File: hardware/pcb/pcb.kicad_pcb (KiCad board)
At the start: 2 copper layers, 122 x 122 mm, 50 parts, among them J1 USB_B_Micro, J2 USB_A, J3 USB_A, J4 USB_A, M1 Fan, Q1 S8050, SW1 SW_Push, U1 locked, U2 AT89C52, U3 SL2.1A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

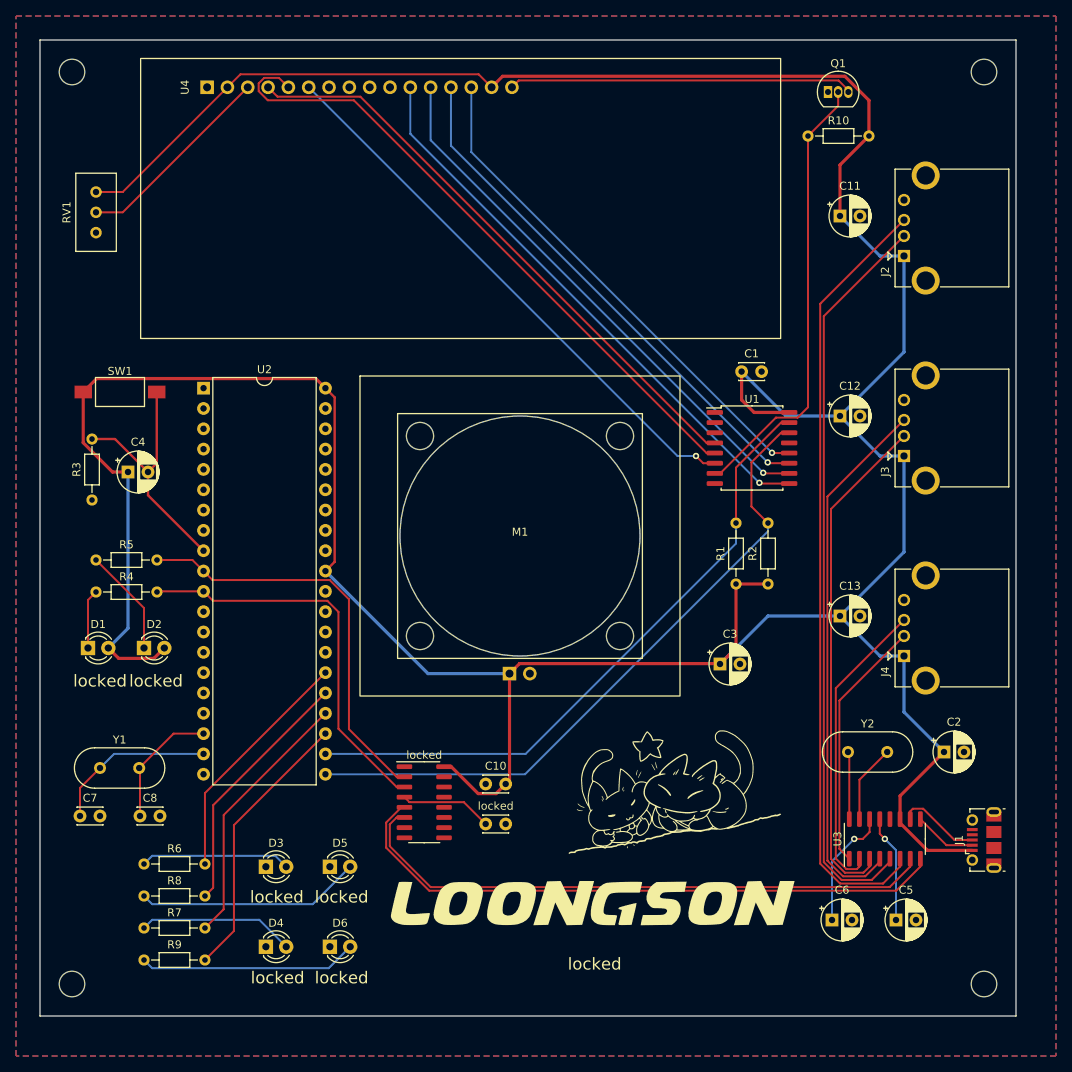
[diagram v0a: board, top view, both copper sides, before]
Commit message: Update KiCAD to 8.0
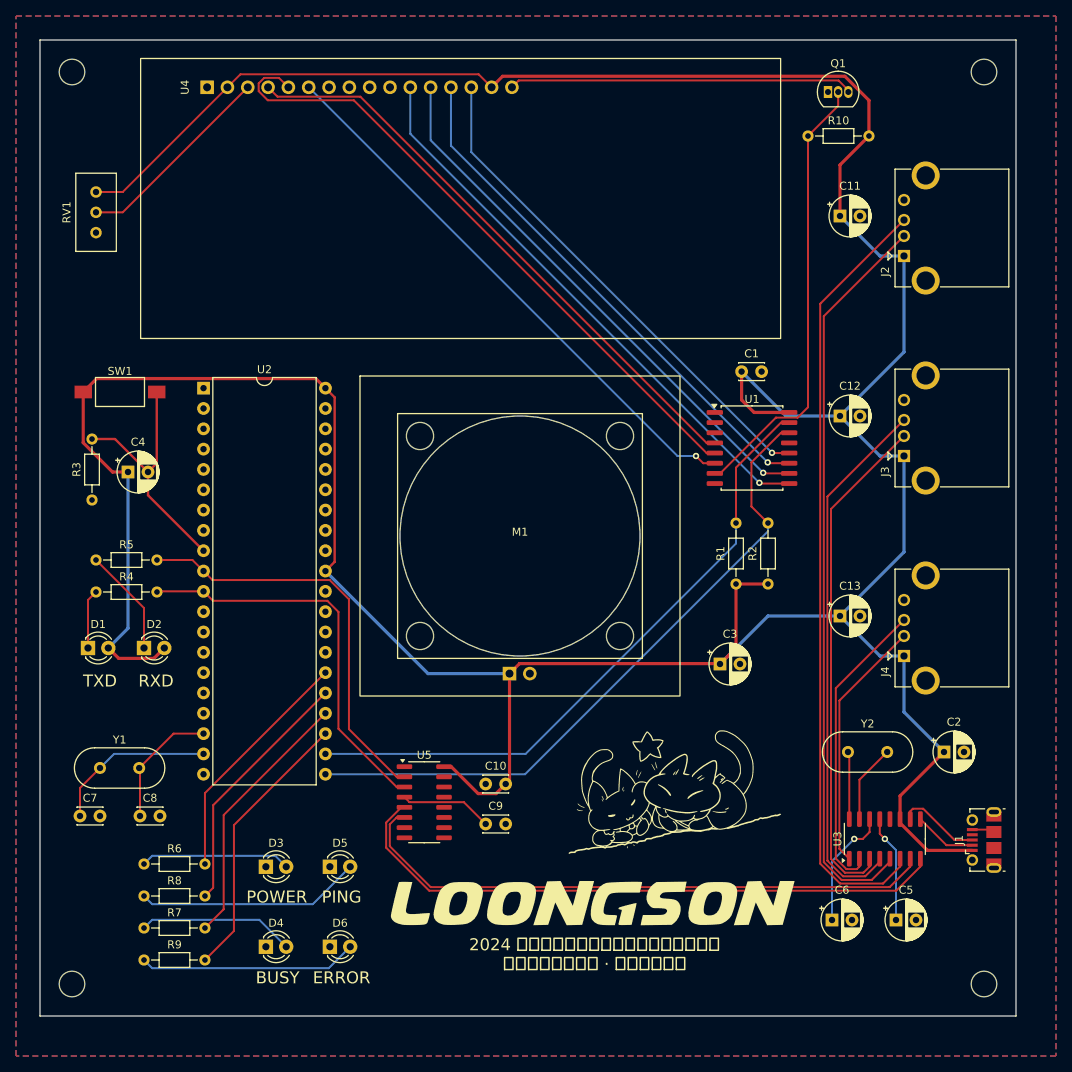
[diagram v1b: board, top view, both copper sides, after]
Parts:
- C12: value locked -> 10uF
- U1: value locked -> PCF8574
- renumbered locked to C9, locked to U5
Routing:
- net GND: track 0.00 -> 2.82 mm
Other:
- board text added: "2024 全国大学生嵌入式芯片与系统设计竞赛 便携式卫星地面站 · 状态显示模组"
- board text added: "BUSY"
- board text added: "ERROR"
- board text added: "PING"
- board text added: "POWER"
- board text added: "RXD"
- board text added: "TXD"
- board text removed: "locked"
